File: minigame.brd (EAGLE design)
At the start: 97.5 x 41.9 mm, 46 parts, among them Q1 MMBT2222A, U1 MCP73831, Y1 8MHz

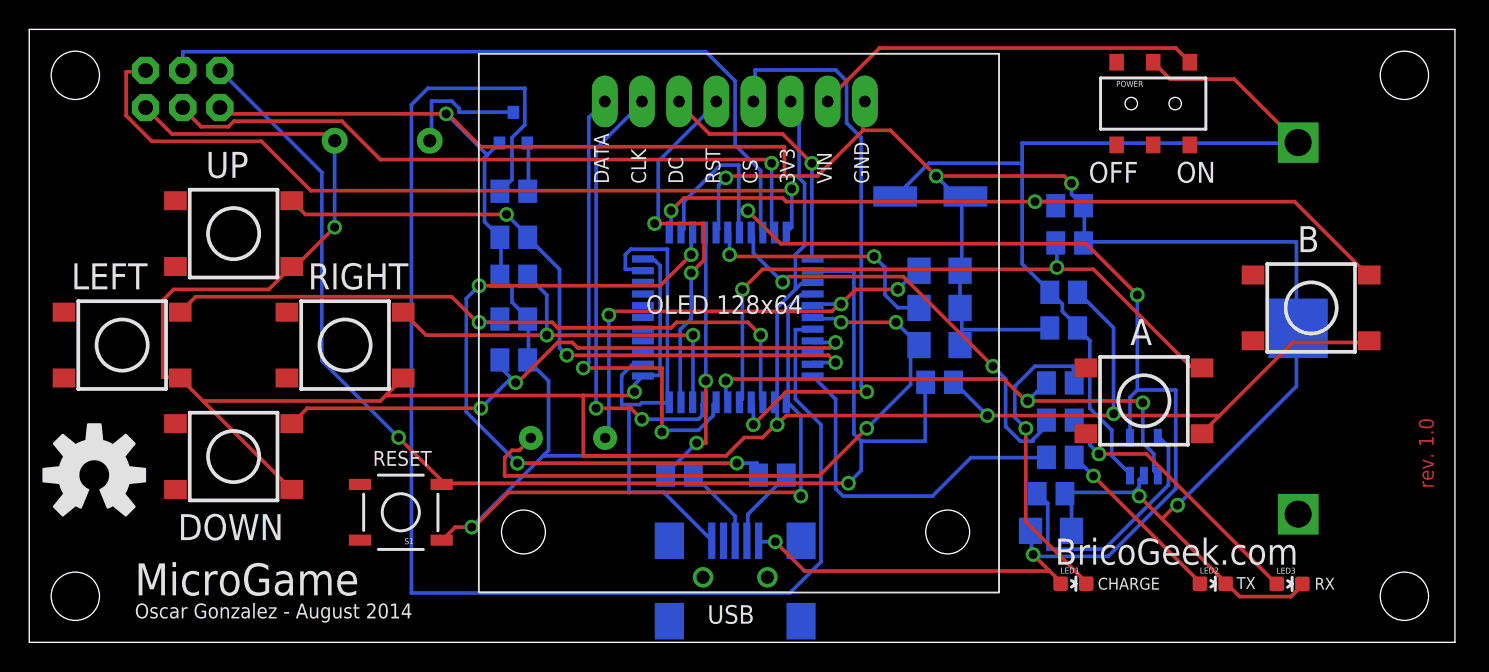
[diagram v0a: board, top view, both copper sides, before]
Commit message: Ground plane in top and bottom
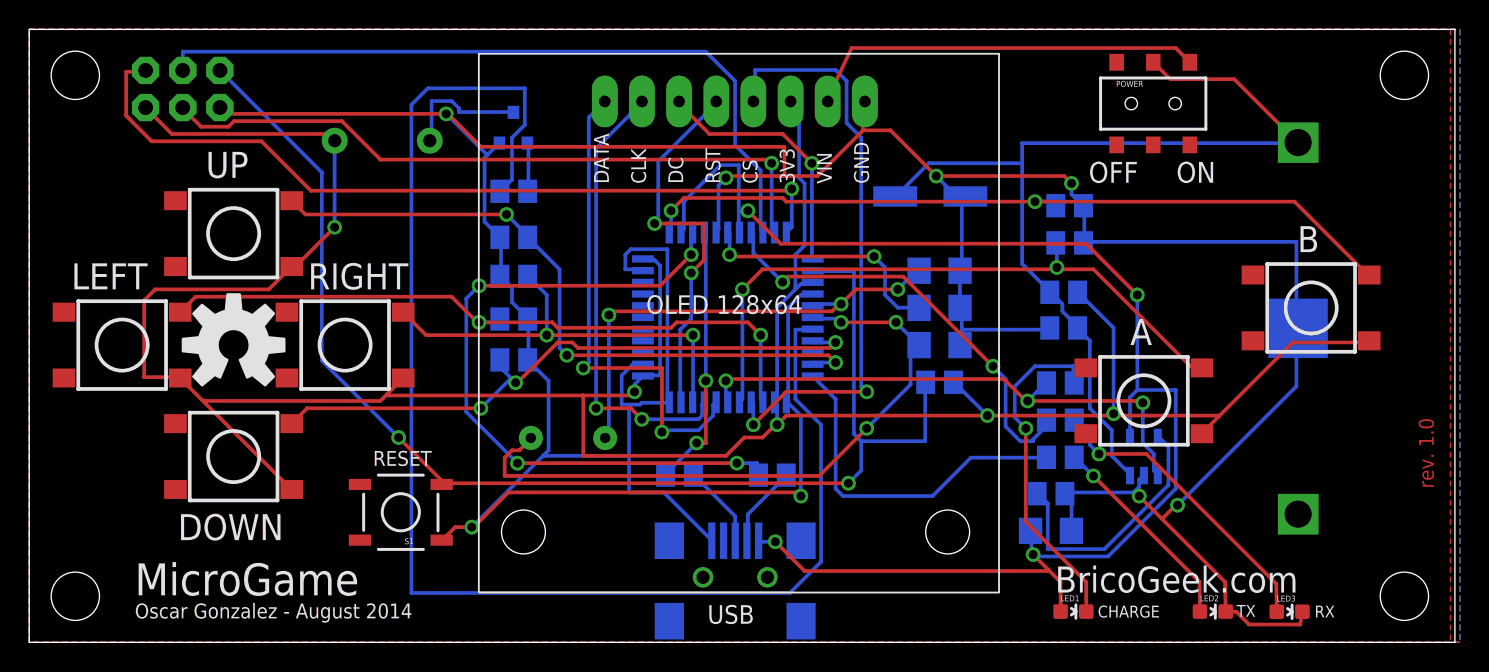
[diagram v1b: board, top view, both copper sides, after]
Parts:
- moved U$3 13.0 mm to (14.0, 20.3)
- moved LED1 1.91 mm to (71.4, 2.10)
- moved LED2 1.90 mm to (80.9, 2.10)
- moved LED3 1.90 mm to (86.2, 2.09)
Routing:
- net 3.3V: track 193.9 -> 196.5 mm
- net GND: track 277.6 -> 279.8 mm
- net VBUS: track 97.5 -> 99.5 mm
- net N$9: track 21.3 -> 23.2 mm
- net N$12: track 12.2 -> 14.1 mm
- net N$13: track 18.8 -> 20.7 mm
- net POWER: track 26.8 -> 27.6 mm
- added copper zone on layer 1, net GND
- added copper zone on layer 16, net GND
- added copper zone on layer 16, net N$10
- added copper zone on layer 1, net N$8

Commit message: Added some stuff to board layout and cleaning
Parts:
- added U$7: (no value), SparkFun-Aesthetics:OSHW-LOGO-L
- moved BAT1 1.27 mm to (88.0, 21.5)
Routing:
- net VBAT: track 66.5 -> 69.0 mm
- net GND: track 279.8 -> 282.3 mm
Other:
- board text added: "1.3' 128x64"
- board text added: "3.6V CR3450"
- board text added: "ATMega32U4 @ 8 MHz"
- board text added: "Arduino compatible!"
- board text added: "Audio buzzer for sound"
- board text added: "Controller:"
- board text added: "Display:"
- board text added: "Embedded Gaming Platform"
- board text added: "Open Source Hardware"
- board text added: "Power:"
- board text added: "Program/Charge"
- board text added: "USB rechargeable"
- board text added: "Use rechargeable CR2450 3.6V Only!"
- board text added: "rev. 1.0 - 12/11/2014"
- board text removed: "Rechargeable CR2450 3.6V Only!"
- board text removed: "rev. 1.0"
